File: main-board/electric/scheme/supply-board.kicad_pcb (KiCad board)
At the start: 2 copper layers, 85 x 56 mm, 139 parts, among them K1 CONN_3, P1 PWR-IN, P10 TST, P11 TST, P12 PWR-IN, P13 CONN_4, P14 PWR-IN, P16 TST, P17 TST, P18 TST, P19 TST, P2 PWR-IN, P3 CONN_4, P4 cross board conn, P5 PWR-IN, P6 TST, P7 TST, P8 TST, P9 CONN_3X2, Q1 BC847, Q10 MOS_N, Q11 MOS_P, Q12 MOS_P, Q2 BC847, Q3 BC847, Q4 MOS_P, Q5 BC847, Q6 BC857, Q7 BC847, Q8 BC857, Q9 BC847, U1 NCP3063, U2 L293, U3 MINI-USB-B, X1 8MHz

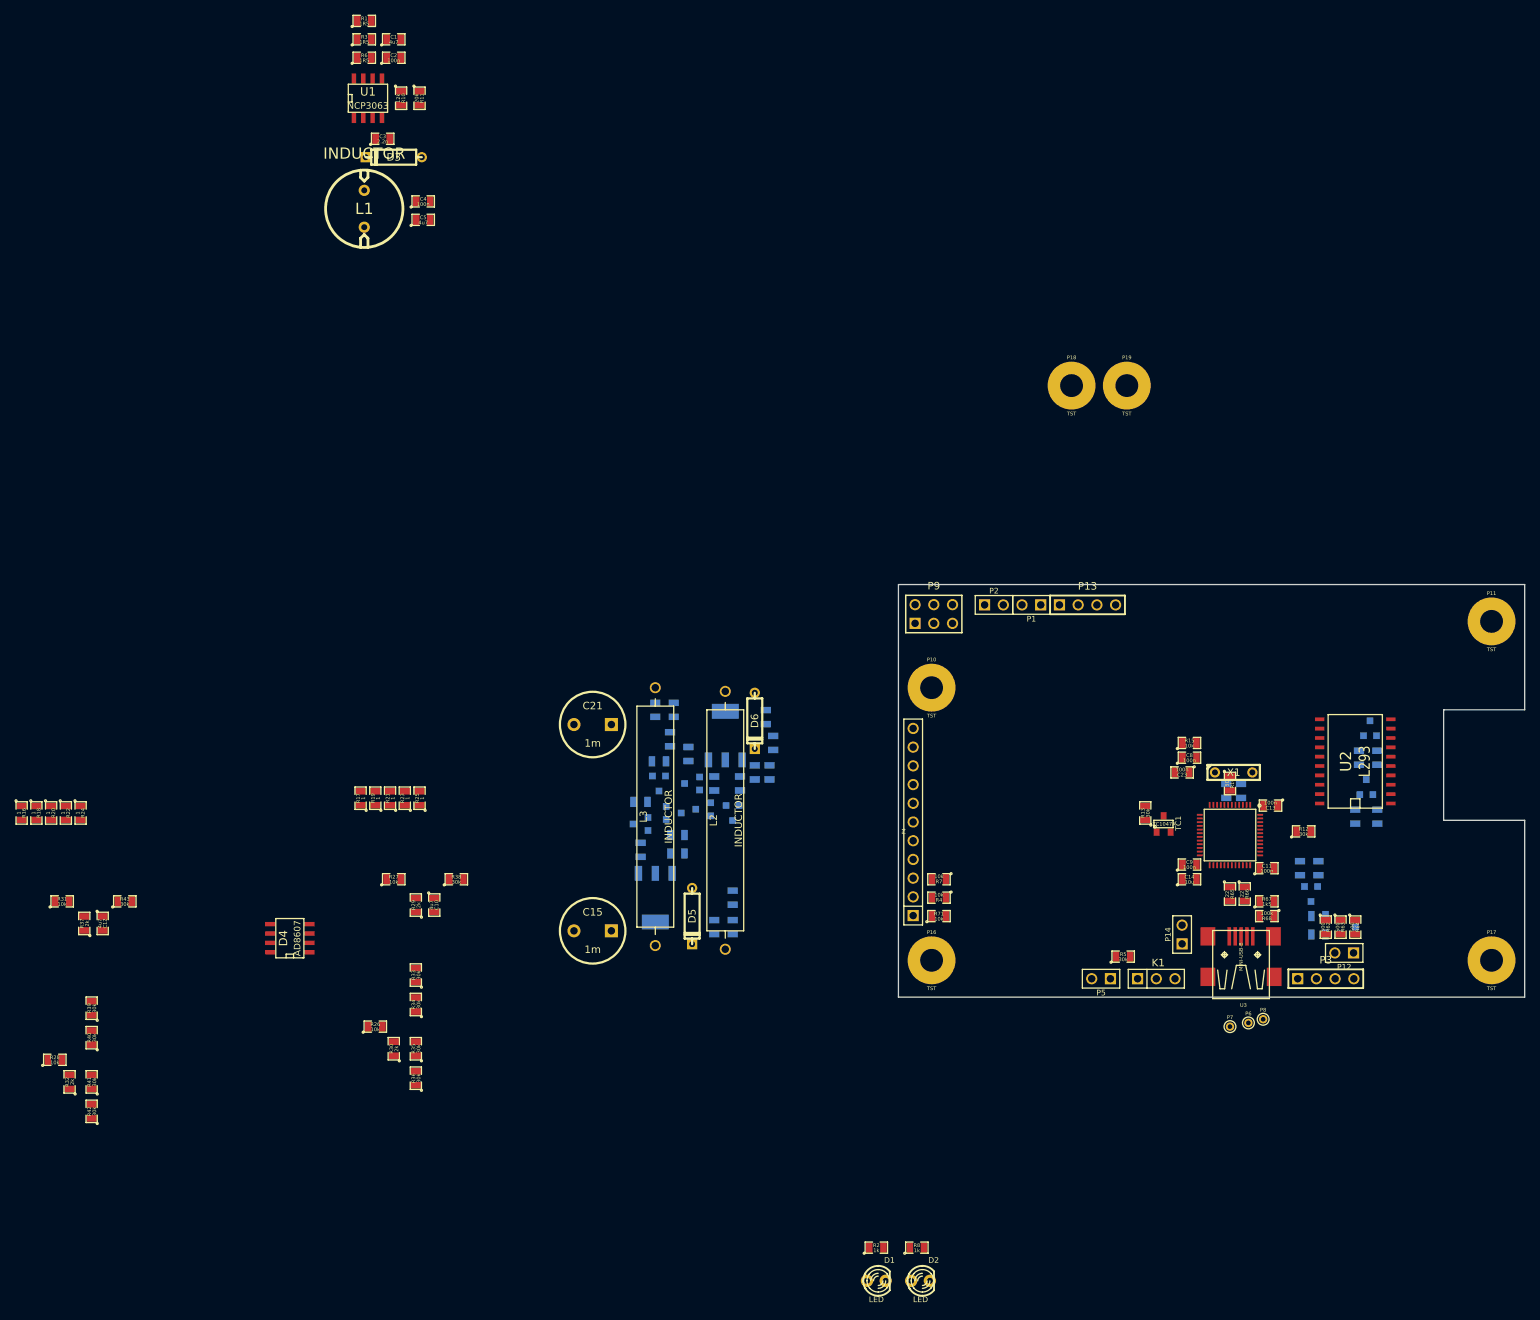
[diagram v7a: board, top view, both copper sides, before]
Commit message: Places all but current measure circuit.
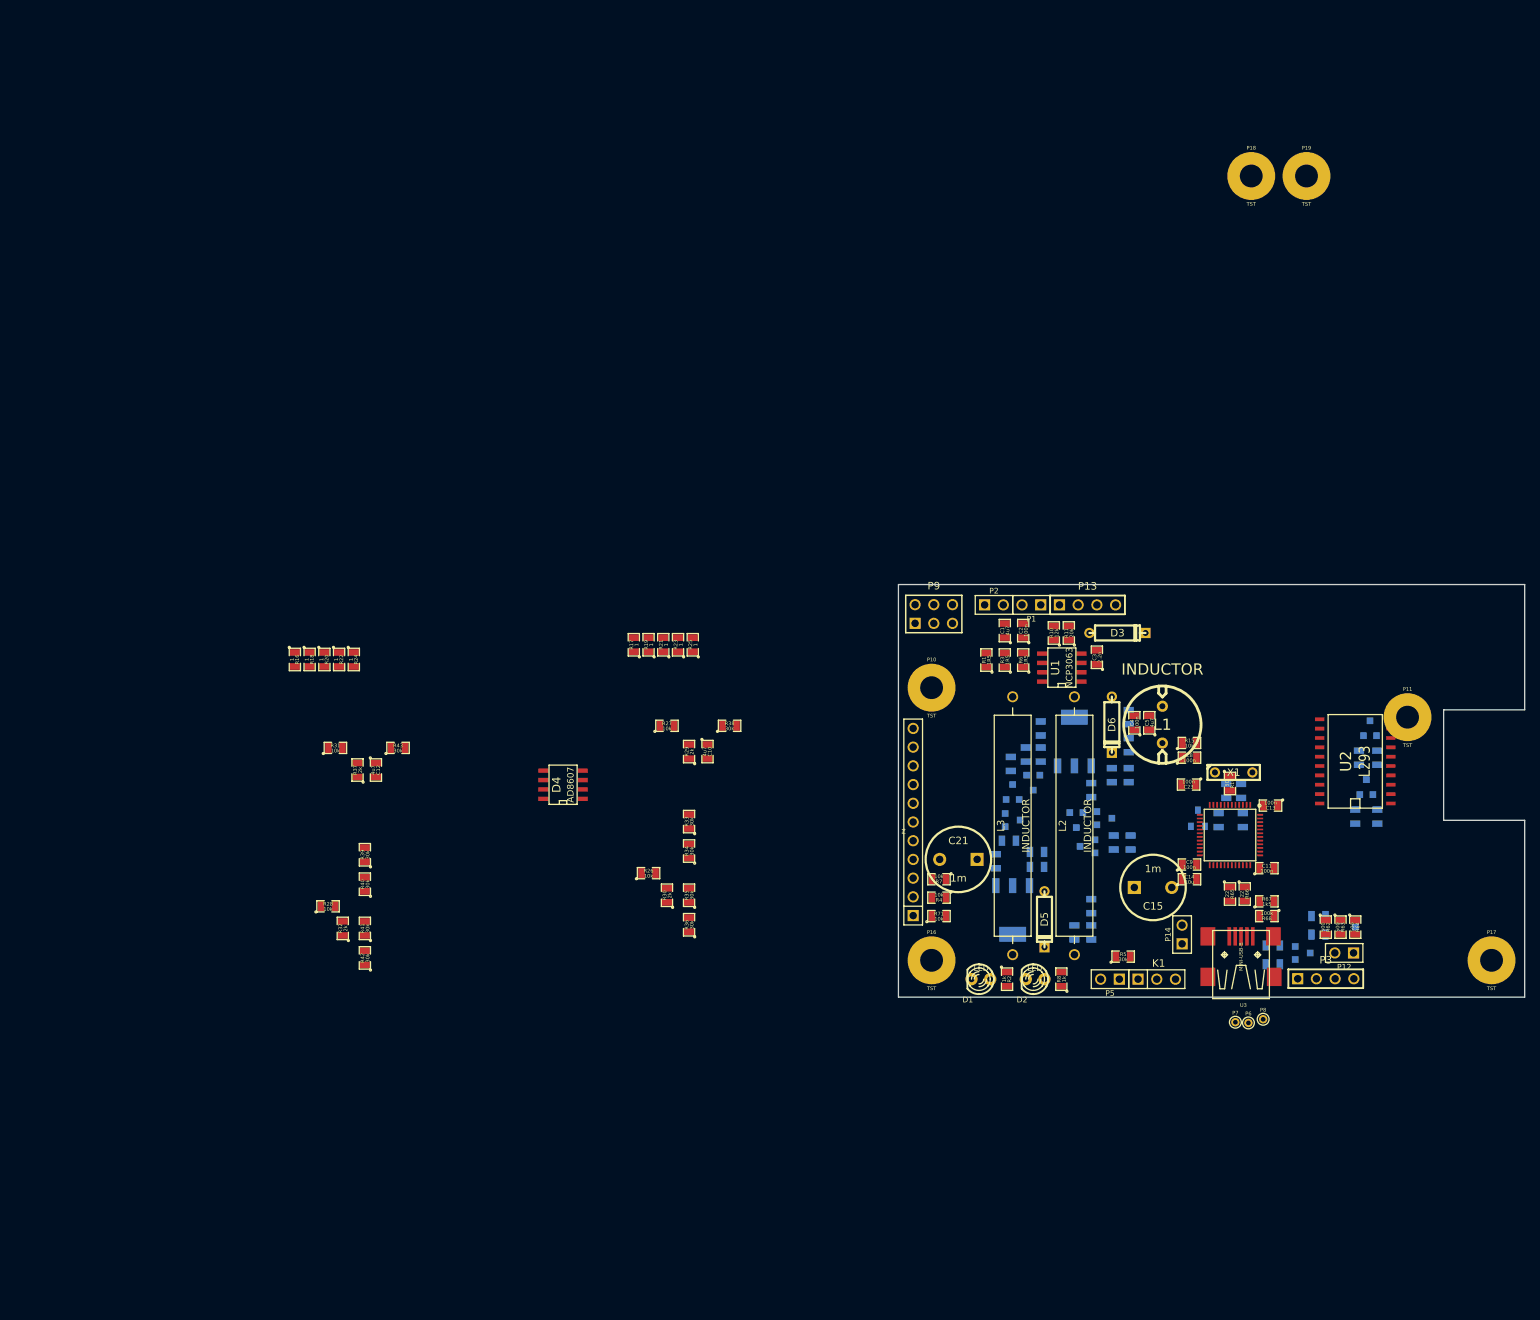
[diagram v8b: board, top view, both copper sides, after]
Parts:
- R12, R13, TC1: moved to B.Cu
- moved L1 129.0 mm to (179.3, 144.0)
- moved U1 121.8 mm to (165.7, 136.3), turned to 90 degrees
- moved R6 121.2 mm to (160.4, 135.2), turned to 90 degrees
- moved R3 121.1 mm to (157.9, 135.2), turned to 90 degrees
- moved R1 121.1 mm to (155.4, 135.2), turned to 90 degrees
- moved C5 119.9 mm to (177.5, 143.8), turned to 90 degrees
- moved C3 119.8 mm to (170.4, 134.9), turned to 90 degrees
- moved C4 119.7 mm to (175.5, 143.8), turned to 90 degrees
- moved D3 117.6 mm to (173.2, 131.6), turned to 0 degrees
- moved C2 115.5 mm to (160.4, 131.2), turned to 90 degrees
- moved C1 115.4 mm to (157.9, 131.2), turned to 90 degrees
- moved R10 114.5 mm to (164.6, 131.6), turned to 90 degrees
- moved R11 114.2 mm to (166.6, 131.6), turned to 90 degrees
- moved C15 76.3 mm to (178.1, 166.1), turned to 0 degrees
- moved R50 61.2 mm to (175.0, 160.0)
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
